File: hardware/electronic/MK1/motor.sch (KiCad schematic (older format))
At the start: 1 part, among them U1 TAMIYA_High_Speed_Gearbox

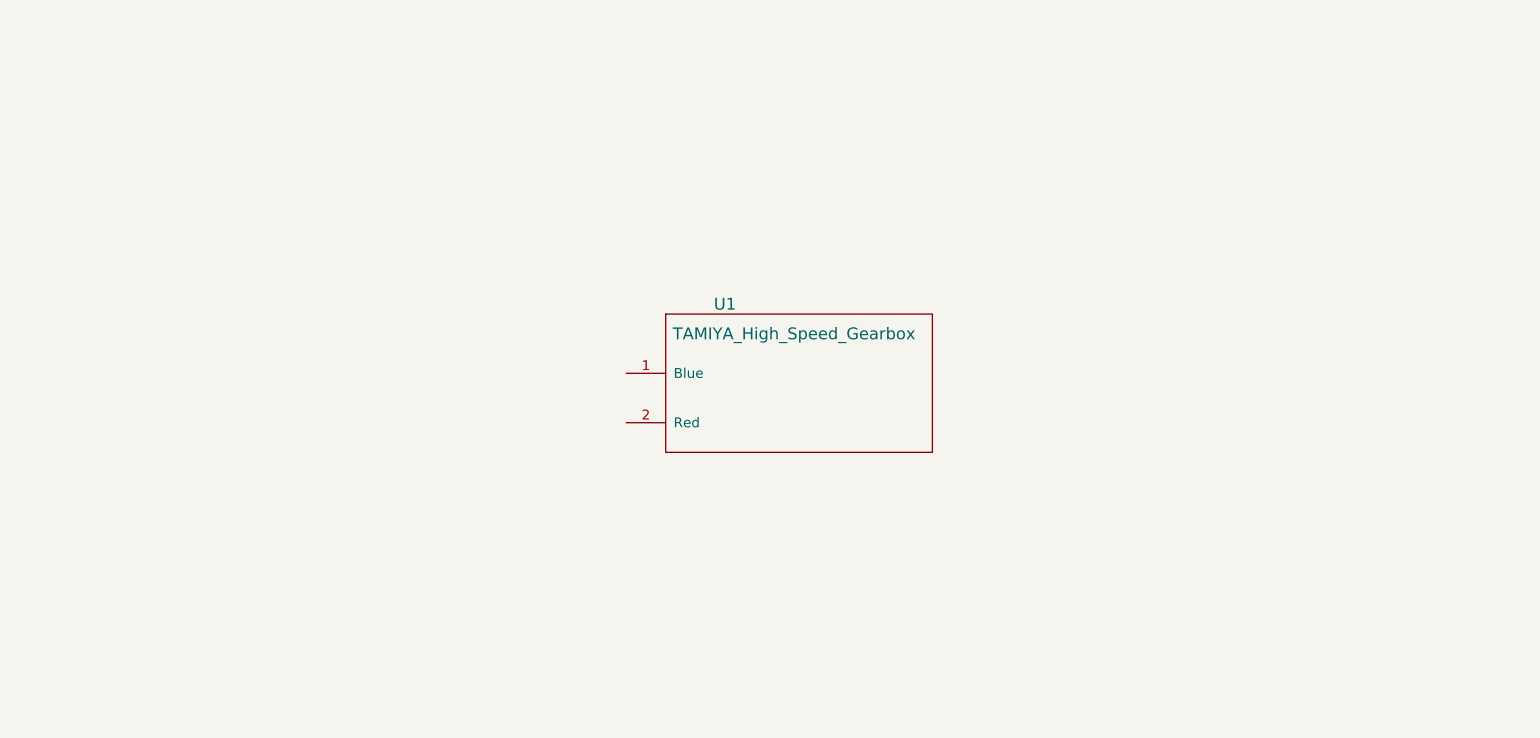
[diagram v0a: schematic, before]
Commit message: HW : Add motor driver IC
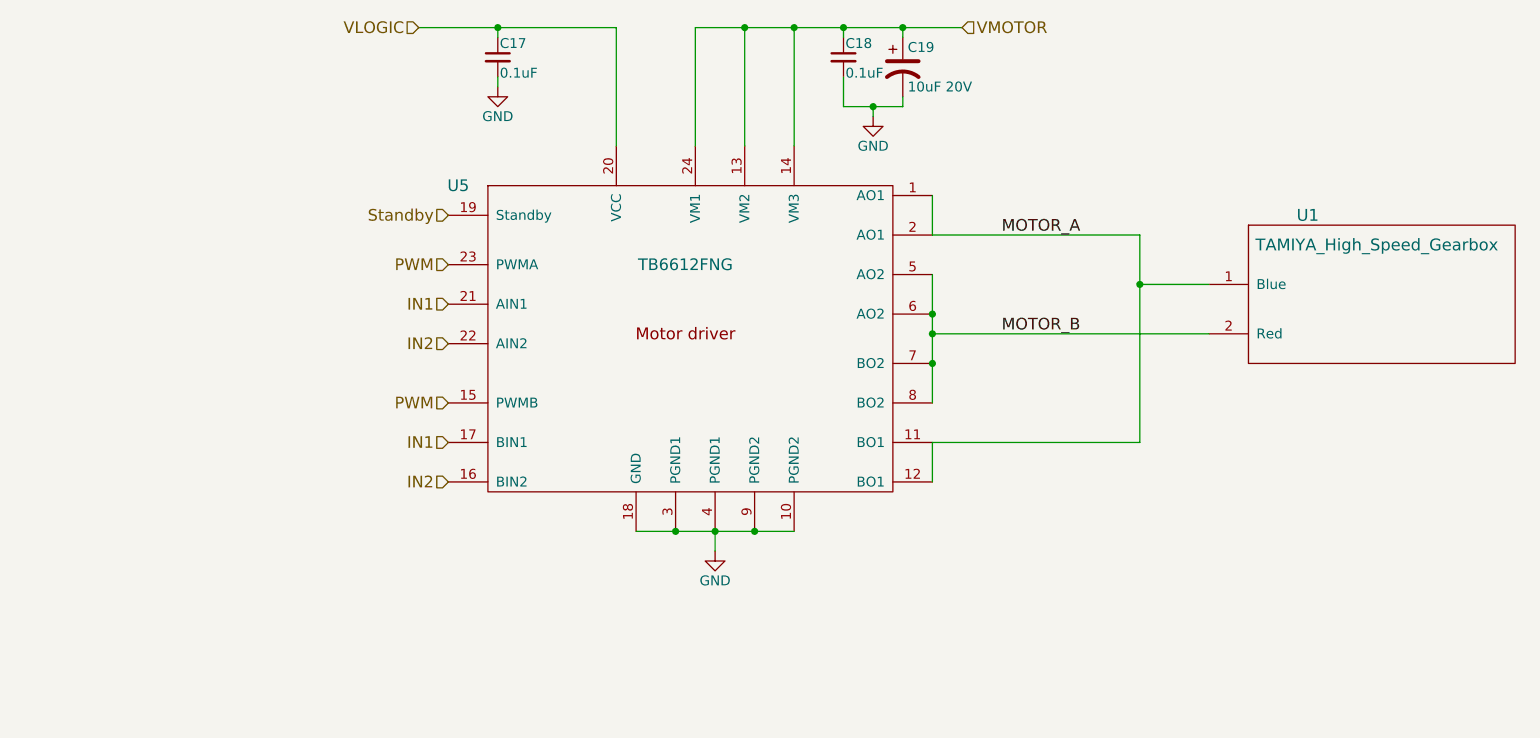
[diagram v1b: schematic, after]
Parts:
- added C17, C18: 0.1uF, Capacitors_SMD:C_0805, symbol C_Small
- added C19: 10uF 20V, Capacitors_Tantalum_SMD:TantalC_SizeT_EIA-3528, symbol CP1
- added U5: TB6612FNG, Housings_SSOP:SSOP-24_5.3x8.2mm_Pitch0.65mm, symbol TB6612FNG
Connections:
- net MOTOR_A: now reaches U1.1 (Blue)
- net MOTOR_A: now also U5.1 (AO1), U5.11 (BO1), U5.12 (BO1), U5.2 (AO1)
- net MOTOR_B: now reaches U1.2 (Red)
- net MOTOR_B: now also U5.5 (AO2), U5.6 (AO2), U5.7 (BO2), U5.8 (BO2)
- new net GND: C17.2, C18.2, C19.2, U5.10 (PGND2), U5.18 (GND), U5.3 (PGND1), U5.4 (PGND1), U5.9 (PGND2)
- new net IN1: U5.17 (BIN1), U5.21 (AIN1)
- new net IN2: U5.16 (BIN2), U5.22 (AIN2)
- new net PWM: U5.15 (PWMB), U5.23 (PWMA)
- new net Standby: U5.19 (Standby)
- new net VLOGIC: C17.1, U5.20 (VCC)
- new net VMOTOR: C18.1, C19.1, U5.13 (VM2), U5.14 (VM3), U5.24 (VM1)
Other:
- moved on the sheet: U1
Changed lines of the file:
@@
 L TAMIYA_High_Speed_Gearbox U1
 U 1 1 5874F75F
-P 5700 3500
-F 0 "U1" H 5300 3600 60  0000 C CNN
-F 1 "TAMIYA_High_Speed_Gearbox" H 5650 3450 60  0000 C CNN
-F 2 "OPAVES_Footprints:TAMIYA_HIgh_Speed_Gearbox" H 5700 3500 60  0001 C CNN
-F 3 "" H 5700 3500 60  0001 C CNN
-	1    5700 3500
+P 8650 3050
+F 0 "U1" H 8250 3150 60  0000 C CNN
+F 1 "TAMIYA_High_Speed_Gearbox" H 8600 3000 60  0000 C CNN
+F 2 "OPAVES_Footprints:TAMIYA_HIgh_Speed_Gearbox" H 8650 3050 60  0001 C CNN
+F 3 "" H 8650 3050 60  0001 C CNN
+	1    8650 3050
 	1    0    0    -1
 $EndComp
+$Comp
+L TB6612FNG U5
+U 1 1 588A9FC9
+P 3950 2800
+F 0 "U5" H 3950 2800 59  0000 C CNN
+F 1 "TB6612FNG" H 5100 2400 59  0000 C CNN
+F 2 "Housings_SSOP:SSOP-24_5.3x8.2mm_Pitch0.65mm" H 3950 2800 59  0001 C CNN
+F 3 "" H 3950 2800 59  0001 C CNN
+	1    3950 2800
+	1    0    0    -1
+$EndComp
+Wire Wire Line
+	6350 3250 6350 3900
+Connection ~ 6350 3700
+Wire Wire Line
+	6350 4100 6350 4300
+Connection ~ 6350 3450
+Wire Wire Line
+	6350 2850 6350 3050
+Text HLabel 3900 3200 0    59   Input ~ 0
+PWM
+Text HLabel 3900 3900 0    59   Input ~ 0
+PWM
+Wire Wire Line
+	4850 4550 5650 4550
+Connection ~ 5050 4550
+Connection ~ 5250 4550
+Connection ~ 5450 4550
+$Comp
+L GND #PWR01
+U 1 1 588AA5AC
+P 5250 4650
+F 0 "#PWR01" H 5250 4400 50  0001 C CNN
+F 1 "GND" H 5250 4500 50  0000 C CNN
+F 2 "" H 5250 4650 50  0000 C CNN
+F 3 "" H 5250 4650 50  0000 C CNN
+	1    5250 4650
+	1    0    0    -1
+$EndComp
+Wire Wire Line
+	5250 4650 5250 4550
+Wire Wire Line
+	7750 3550 6350 3550
+Connection ~ 6350 3550
+Wire Wire Line
+	7400 4100 6350 4100
+Wire Wire Line
+	7400 3050 7400 4100
+Wire Wire Line
+	7400 3300 7750 3300
+Wire Wire Line
+	6350 3050 7400 3050
+Connection ~ 7400 3300
+Text HLabel 3900 3400 0    59   Input ~ 0
+IN1
+Text HLabel 3900 4100 0    59   Input ~ 0
+IN1
+Text HLabel 3900 3600 0    59   Input ~ 0
+IN2
+Text HLabel 3900 4300 0    59   Input ~ 0
+IN2
+Text HLabel 3900 2950 0    59   Input ~ 0
+Standby
+Text HLabel 6500 2000 2    59   Input ~ 0
+VMOTOR
+Text HLabel 3750 2000 0    59   Input ~ 0
+VLOGIC
+$Comp
+L C_Small C17
+U 1 1 588AD03F
+P 4150 2150
+F 0 "C17" H 4160 2220 50  0000 L CNN
+F 1 "0.1uF" H 4160 2070 50  0000 L CNN
+F 2 "Capacitors_SMD:C_0805" H 4150 2150 50  0001 C CNN
+F 3 "" H 4150 2150 50  0000 C CNN
+	1    4150 2150
+	1    0    0    -1
+$EndComp
+Wire Wire Line
+	4750 2000 4750 2600
+$Comp
+L GND #PWR02
+U 1 1 588AD1AC
+P 4150 2300
+F 0 "#PWR02" H 4150 2050 50  0001 C CNN
+F 1 "GND" H 4150 2150 50  0000 C CNN
+F 2 "" H 4150 2300 50  0000 C CNN
+F 3 "" H 4150 2300 50  0000 C CNN
+	1    4150 2300
+	1    0    0    -1
+$EndComp
+Wire Wire Line
+	4750 2000 3750 2000
+Connection ~ 4150 2000
+Wire Wire Line
+	4150 2300 4150 2250
+Wire Wire Line
+	4150 2050 4150 2000
+Wire Wire Line
+	6500 2000 5150 2000
+Wire Wire Line
+	5150 2000 5150 2600
+Wire Wire Line
+	5400 2600 5400 2000
+Connection ~ 5400 2000
+Wire Wire Line
+	5650 2600 5650 2000
+Connection ~ 5650 2000
+$Comp
+L C_Small C18
+U 1 1 588AD5D1
+P 5900 2150
+F 0 "C18" H 5910 2220 50  0000 L CNN
+F 1 "0.1uF" H 5910 2070 50  0000 L CNN
+F 2 "Capacitors_SMD:C_0805" H 5900 2150 50  0001 C CNN
+F 3 "" H 5900 2150 50  0000 C CNN
+	1    5900 2150
+	1    0    0    -1
+$EndComp
+Wire Wire Line
+	6200 2050 6200 2000
+Connection ~ 6200 2000
+$Comp
+L CP1 C19
+U 1 1 588AD684
+P 6200 2200
+F 0 "C19" H 6225 2300 50  0000 L CNN
+F 1 "10uF 20V" H 6225 2100 50  0000 L CNN
+F 2 "Capacitors_Tantalum_SMD:TantalC_SizeT_EIA-3528" H 6200 2200 50  0001 C CNN
+F 3 "" H 6200 2200 50  0000 C CNN
+	1    6200 2200
+	1    0    0    -1
+$EndComp
+Wire Wire Line
+	5900 2050 5900 2000
+Connection ~ 5900 2000
+Wire Wire Line
+	5900 2400 6200 2400
+Wire Wire Line
+	6050 2400 6050 2450
+Connection ~ 6050 2400
+$Comp
+L GND #PWR03
+U 1 1 588AD740
+P 6050 2450
+F 0 "#PWR03" H 6050 2200 50  0001 C CNN
+F 1 "GND" H 6050 2300 50  0000 C CNN
+F 2 "" H 6050 2450 50  0000 C CNN
+F 3 "" H 6050 2450 50  0000 C CNN
+	1    6050 2450
+	1    0    0    -1
+$EndComp
+Wire Wire Line
+	6200 2400 6200 2350
+Wire Wire Line
+	5900 2400 5900 2250
+Text Label 6700 3050 0    59   ~ 0
+MOTOR_A
+Text Label 6700 3550 0    59   ~ 0
+MOTOR_B
 $EndSCHEMATC

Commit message: HW: Signal assignment and routing cont.
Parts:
- added Encoder1: CONN_01X04, Pin_Headers:Pin_Header_Straight_1x04, symbol CONN_01X04
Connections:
- net GND: now also Encoder1.2 (P2)
- net VLOGIC: now also Encoder1.1 (P1)
- new net Encoder_A: Encoder1.3 (P3)
- new net Encoder_B: Encoder1.4 (P4)
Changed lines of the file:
@@
 Connection ~ 5450 4550
 $Comp
-L GND #PWR3
+L GND #PWR02
 U 1 1 588AA5AC
 P 5250 4650
-F 0 "#PWR3" H 5250 4400 50  0001 C CNN
+F 0 "#PWR02" H 5250 4400 50  0001 C CNN
 F 1 "GND" H 5250 4500 50  0000 C CNN
 F 2 "" H 5250 4650 50  0000 C CNN
@@
 	4750 2000 4750 2600
 $Comp
-L GND #PWR2
+L GND #PWR03
 U 1 1 588AD1AC
 P 4150 2300
-F 0 "#PWR2" H 4150 2050 50  0001 C CNN
+F 0 "#PWR03" H 4150 2050 50  0001 C CNN
 F 1 "GND" H 4150 2150 50  0000 C CNN
 F 2 "" H 4150 2300 50  0000 C CNN
@@
 Connection ~ 6050 2400
 $Comp
-L GND #PWR4
+L GND #PWR04
 U 1 1 588AD740
 P 6050 2450
-F 0 "#PWR4" H 6050 2200 50  0001 C CNN
+F 0 "#PWR04" H 6050 2200 50  0001 C CNN
 F 1 "GND" H 6050 2300 50  0000 C CNN
 F 2 "" H 6050 2450 50  0000 C CNN
@@
 Text Label 6700 3550 0    59   ~ 0
 MOTOR_B
+Text HLabel 2000 4900 3    60   Input ~ 0
+Encoder_A
+$Comp
+L CONN_01X04 Encoder1
+U 1 1 5893DD3A
+P 1950 4700
+F 0 "Encoder1" V 2050 4700 50  0000 C CNN
+F 1 "CONN_01X04" V 2050 4700 50  0001 C CNN
+F 2 "Pin_Headers:Pin_Header_Straight_1x04" H 1950 4700 50  0001 C CNN
+F 3 "" H 1950 4700 50  0000 C CNN
+	1    1950 4700
+	0    -1   -1   0
+$EndComp
+Text HLabel 2100 4900 3    60   Input ~ 0
+Encoder_B
+Text HLabel 1800 4900 3    59   Input ~ 0
+VLOGIC
+$Comp
+L GND #PWR05
+U 1 1 5893DF17
+P 1900 4900
+F 0 "#PWR05" H 1900 4650 50  0001 C CNN
+F 1 "GND" H 1900 4750 50  0000 C CNN
+F 2 "" H 1900 4900 50  0000 C CNN
+F 3 "" H 1900 4900 50  0000 C CNN
+	1    1900 4900
+	1    0    0    -1
+$EndComp
 $EndSCHEMATC

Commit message: HW: Add missing component values
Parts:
- C17, C18: value 0.1uF -> 100nF
- Encoder1: value CONN_01X04 -> MOLEX 22-28-5044
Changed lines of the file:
@@
 P 4150 2150
 F 0 "C17" H 4160 2220 50  0000 L CNN
-F 1 "0.1uF" H 4160 2070 50  0000 L CNN
+F 1 "100nF" H 4160 2070 50  0000 L CNN
 F 2 "Capacitors_SMD:C_0805" H 4150 2150 50  0001 C CNN
 F 3 "" H 4150 2150 50  0000 C CNN
@@
 P 5900 2150
 F 0 "C18" H 5910 2220 50  0000 L CNN
-F 1 "0.1uF" H 5910 2070 50  0000 L CNN
+F 1 "100nF" H 5910 2070 50  0000 L CNN
 F 2 "Capacitors_SMD:C_0805" H 5900 2150 50  0001 C CNN
 F 3 "" H 5900 2150 50  0000 C CNN
@@
 P 1950 4700
 F 0 "Encoder1" V 2050 4700 50  0000 C CNN
-F 1 "CONN_01X04" V 2050 4700 50  0001 C CNN
+F 1 "MOLEX 22-28-5044" V 2050 4700 50  0001 C CNN
 F 2 "Pin_Headers:Pin_Header_Straight_1x04" H 1950 4700 50  0001 C CNN
 F 3 "" H 1950 4700 50  0000 C CNN
